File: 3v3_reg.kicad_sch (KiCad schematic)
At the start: 15 parts, among them U7 TPS62A01PDDCR

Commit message: did stuff, amongst others changed to op-amp input filter
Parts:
- D79, D81: value D_Schottky -> DSL34; LCSC (none) -> C22466347; LCSC Basic/Pref (none) -> n; LCSC Part (none) -> C22466347
- U7: footprint TPS62A01PDDCR:DDC0006A-MFG -> TPS62A01PDDCR:DDC0006A-IPC_A; LCSC (none) -> C42267816

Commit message: did stuff
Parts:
- R81, R82: LCSC Basic/Pref x -> y
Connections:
- net +5.2V renamed +5.3V
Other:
- note removed: "todo: change to C22466347"
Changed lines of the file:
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@@
 	(generator_version "10.0")
 	(paper "A4")
-	(text "todo: change to C22466347"
-		(exclude_from_sim no)
-		(at 24.384 87.376 0)
-		(effects
-			(font
-				(size 1.27 1.27)
-			)
-		)
-	)
 	(text "3.3 V Regulator"
 		(exclude_from_sim no)
@@
 		)
 	)
-	(text_box "Design Note:\nPrioritizes 5.2 V \nfrom the Ethernet PoE\nover 5.0 V from USB"
+	(text_box "Design Note:\nPrioritizes 5.3 V \nfrom the Ethernet PoE\nover 5.0 V from USB"
 		(exclude_from_sim no)
 		(at 44.45 57.15 0)
@@
 			)
 		)
-		(property "LCSC Basic/Pref" "x"
+		(property "LCSC Basic/Pref" "y"
 			(at 93.98 100.33 0)
 			(hide yes)
@@
 			)
 		)
-		(property "LCSC Basic/Pref" "x"
+		(property "LCSC Basic/Pref" "y"
 			(at 177.8 97.79 0)
 			(hide yes)
@@
 		(in_pos_files yes)
 		(dnp no)
-		(fields_autoplaced yes)
 		(property "Reference" "#PWR0324"
 			(at 43.18 83.82 0)
@@
 			)
 		)
-		(property "Value" "+5.2V"
-			(at 43.18 74.93 0)
-			(show_name no)
-			(do_not_autoplace no)
-			(effects
-				(font
-					(size 1.27 1.27)
-				)
-			)
-		)
+		(property "Value" "+5.3V"
+			(at 41.148 76.2 0)
+			(show_name no)
+			(do_not_autoplace no)
+			(effects
+				(font
+					(size 1.27 1.27)
+				)
+				(justify left)
+			)
+		)

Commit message: fixed leds
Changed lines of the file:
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@@
 	)
 	(junction
+		(at 76.2 92.71)
+		(diameter 0)
+		(color 0 0 0 0)
+	)
+	(junction
 		(at 220.98 92.71)
 		(diameter 0)
@@
 	(wire
 		(pts
+			(xy 76.2 92.71) (xy 80.01 92.71)
+		)
+		(stroke
+			(width 0)
+			(type default)
+		)
+	)
+	(wire
+		(pts
 			(xy 220.98 92.71) (xy 220.98 93.98)
 		)
@@
 	(wire
 		(pts
+			(xy 76.2 87.63) (xy 76.2 92.71)
+		)
+		(stroke
+			(width 0)
+			(type default)
+		)
+	)
+	(wire
+		(pts
 			(xy 177.8 92.71) (xy 195.58 92.71)
 		)
@@
 	(wire
 		(pts
-			(xy 63.5 92.71) (xy 80.01 92.71)
+			(xy 63.5 92.71) (xy 76.2 92.71)
 		)
 		(stroke
@@
 		)
 	)
-	(label "V3P3_VIN"
-		(at 71.12 92.71 0)
-		(effects
-			(font
-				(size 1.27 1.27)
-			)
-			(justify left bottom)
-		)
-	)
 	(label "3V3_EN"
 		(at 95.25 107.95 0)
@@
 					(unit 1)
 				)
+			)
+		)
+	)
+	(symbol
+		(lib_id "power:+3.3V")
+		(at 76.2 87.63 0)
+		(unit 1)
+		(body_style 1)
+		(exclude_from_sim no)
+		(in_bom yes)
+		(on_board yes)
+		(in_pos_files yes)
+		(dnp no)
+		(property "Reference" "#PWR0547"
+			(at 76.2 91.44 0)
+			(hide yes)
+			(show_name no)
+			(do_not_autoplace no)
+			(effects
+				(font
+					(size 1.27 1.27)
+				)
+			)
+		)
+		(property "Value" "V3P3_VIN"
+			(at 72.136 83.82 0)
+			(show_name no)
+			(do_not_autoplace no)
+			(effects
+				(font
+					(size 1.27 1.27)
+				)
+				(justify left)
+			)
+		)
+		(property "Footprint" ""
+			(at 76.2 87.63 0)
+			(hide yes)
+			(show_name no)
+			(do_not_autoplace no)
+			(effects
+				(font
+					(size 1.27 1.27)
+				)
+			)
+		)
+		(property "Datasheet" ""
+			(at 76.2 87.63 0)
+			(hide yes)
+			(show_name no)
+			(do_not_autoplace no)
+			(effects
+				(font
+					(size 1.27 1.27)
+				)
+			)
+		)
+		(property "Description" "Power symbol creates a global label with name \"+3.3V\""
+			(at 76.2 87.63 0)
+			(hide yes)
+			(show_name no)
+			(do_not_autoplace no)
+			(effects
+				(font
+					(size 1.27 1.27)
+				)
+			)
+		)
+		(pin "1"
+		)
+		(instances
+			(project "netdaq"
+				(path "/2970f661-65ab-4e2b-aeda-d76d1044f2b8/4a874178-a54c-4eb4-8350-ff261e3dfdab"
+					(reference "#PWR0547")
+					(unit 1)
+				)

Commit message: fixed a lot of review comments
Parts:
- D79: MPN (none) -> DSL34; Manufacturer (none) -> hongjiacheng
- R81, R82: Tolerance (none) -> 1%
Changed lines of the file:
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@@
 			)
 		)
-		(property "Tolerance" ""
+		(property "Tolerance" "1%"
 			(at 93.98 100.33 0)
 			(hide yes)
@@
 			)
 		)
+		(property "MPN" "DSL34"
+			(at 54.61 82.55 0)
+			(hide yes)
+			(show_name no)
+			(do_not_autoplace no)
+			(effects
+				(font
+					(size 1.27 1.27)
+				)
+			)
+		)
+		(property "Manufacturer" "hongjiacheng"
+			(at 54.61 82.55 0)
+			(hide yes)
+			(show_name no)
+			(do_not_autoplace no)
+			(effects
+				(font
+					(size 1.27 1.27)
+				)
+			)
+		)
 		(pin "1"
 		)
@@
 			)
 		)
-		(property "Tolerance" ""
+		(property "Tolerance" "1%"
 			(at 177.8 97.79 0)
 			(hide yes)

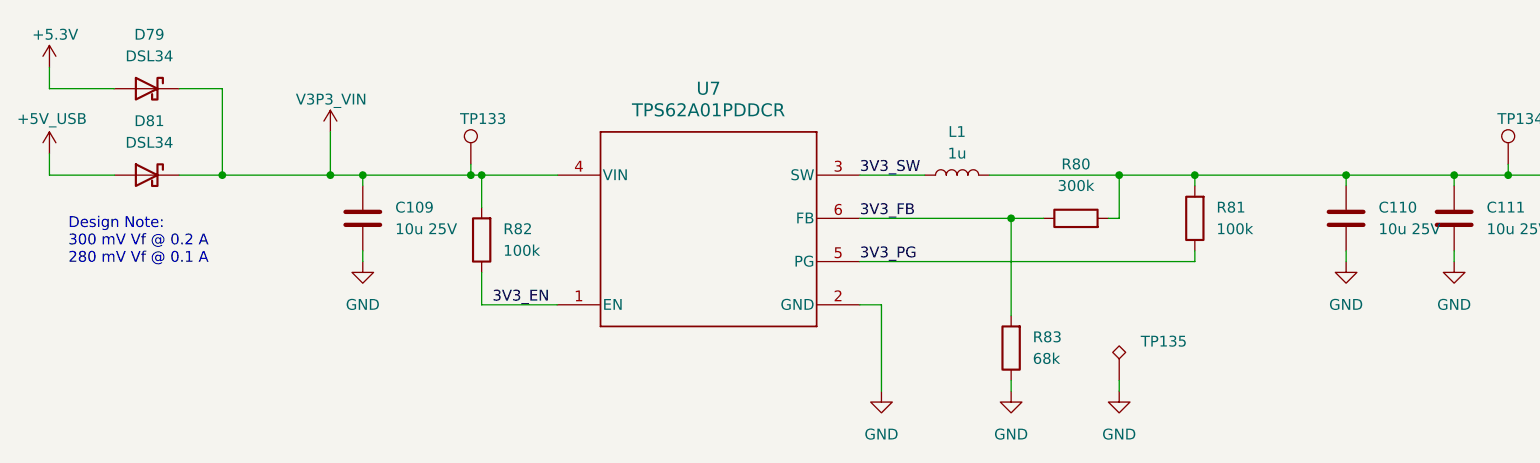
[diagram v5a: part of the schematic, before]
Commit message: fixed some more schematic review
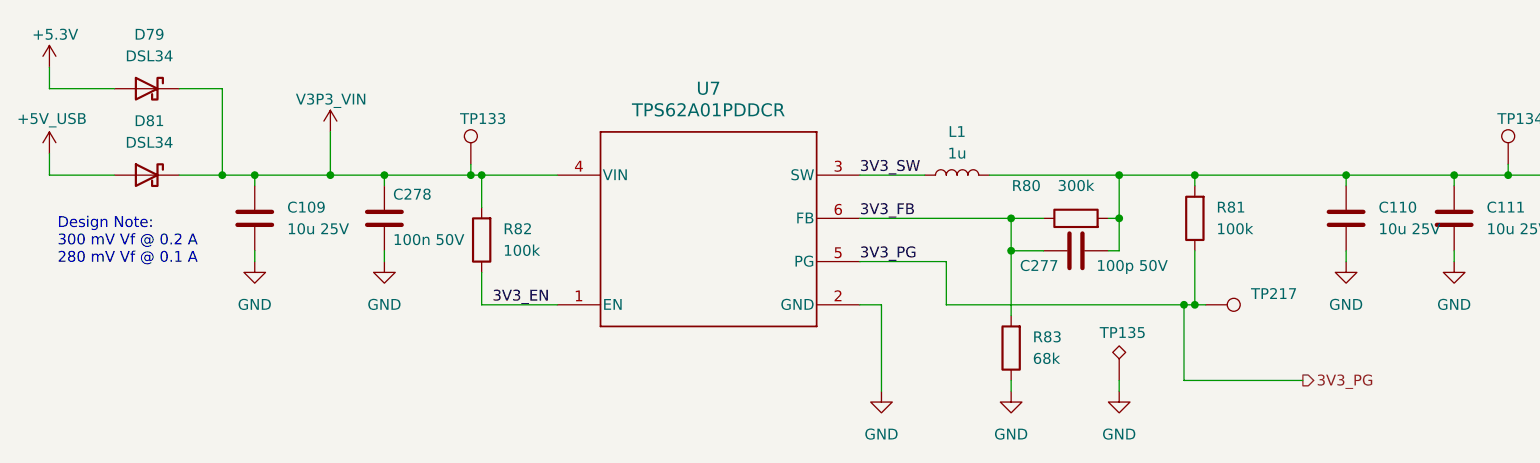
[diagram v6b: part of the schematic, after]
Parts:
- added C277: 100p 50V, Capacitor_SMD:C_0402_1005Metric, symbol Device:C
- added C278: 100n 50V, Capacitor_SMD:C_0402_1005Metric, symbol Device:C
- added TP217: TestPoint, TestPoint:TestPoint_THTPad_D1.0mm_Drill0.5mm, symbol Connector:TestPoint
- C109, C110, C111, C112: LCSC Basic/Pref x -> basic; LCSC missing (none) -> n; MPN (none) -> CL21A106KAYNNNE; Manufacturer (none) -> Samsung Electro-Mechanics; TC (none) -> X5R; Tolerance (none) -> 10%; Voltage (none) -> 25V
- D79: LCSC Basic/Pref n -> preferred; LCSC missing (none) -> n
- D81: LCSC Basic/Pref n -> preferred; LCSC missing (none) -> n; MPN (none) -> DSL34; Manufacturer (none) -> hongjiacheng
- L1: footprint Inductor_SMD:L_1210_3225Metric -> Inductor_SMD:L_1008_2520Metric; LCSC (none) -> C435392; LCSC Basic/Pref (none) -> extended; LCSC Part (none) -> C435392; LCSC missing (none) -> n; MPN (none) -> DFE252012F-1R0M=P2; Manufacturer (none) -> Murata Electronics
- R80: LCSC Basic/Pref x -> basic; LCSC missing (none) -> n; MPN (none) -> 0603WAF3003T5E; Manufacturer (none) -> UNI-ROYAL(Uniroyal Elec); Power (none) -> 100mW; Tolerance (none) -> 1%; Voltage (none) -> 75V
- R81, R82: LCSC Basic/Pref y -> basic; LCSC missing (none) -> n; MPN (none) -> 0402WGF1003TCE; Manufacturer (none) -> UNI-ROYAL(Uniroyal Elec); Power (none) -> 62.5mW; Voltage (none) -> 50V
- R83: LCSC Basic/Pref x -> basic; LCSC missing (none) -> n; MPN (none) -> 0603WAF6802T5E; Manufacturer (none) -> UNI-ROYAL(Uniroyal Elec); Power (none) -> 100mW; Tolerance (none) -> 1%; Voltage (none) -> 75V
- U7: LCSC Basic/Pref (none) -> extended; LCSC missing (none) -> n; MPN (none) -> TPS62A01PDDCR; Manufacturer (none) -> TEXAS INSTRUMENTS
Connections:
- net +3.3V: now also C277.2
- net 3V3_FB: now also C277.1
- net 3V3_PG: now also TP217.1
- net GND: now also C278.2
- net V3P3_VIN: now also C278.1
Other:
- moved on the sheet: C109

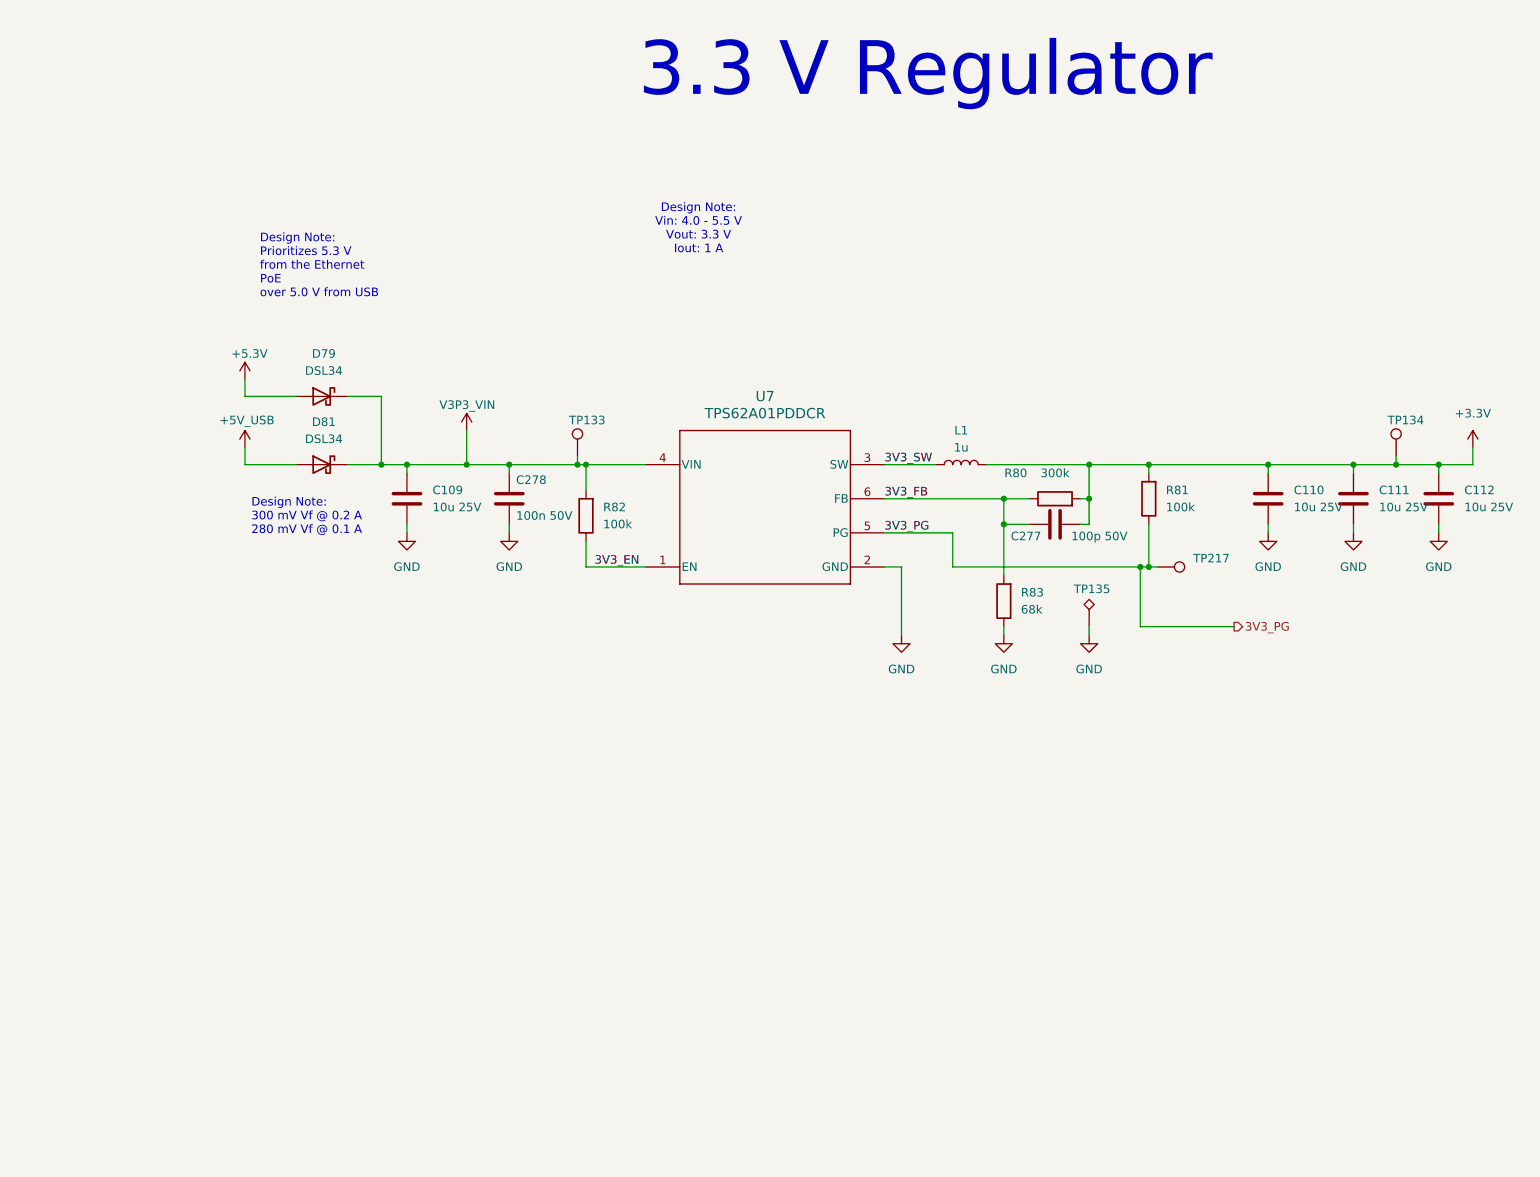
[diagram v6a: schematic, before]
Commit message: fixed some more schematic review
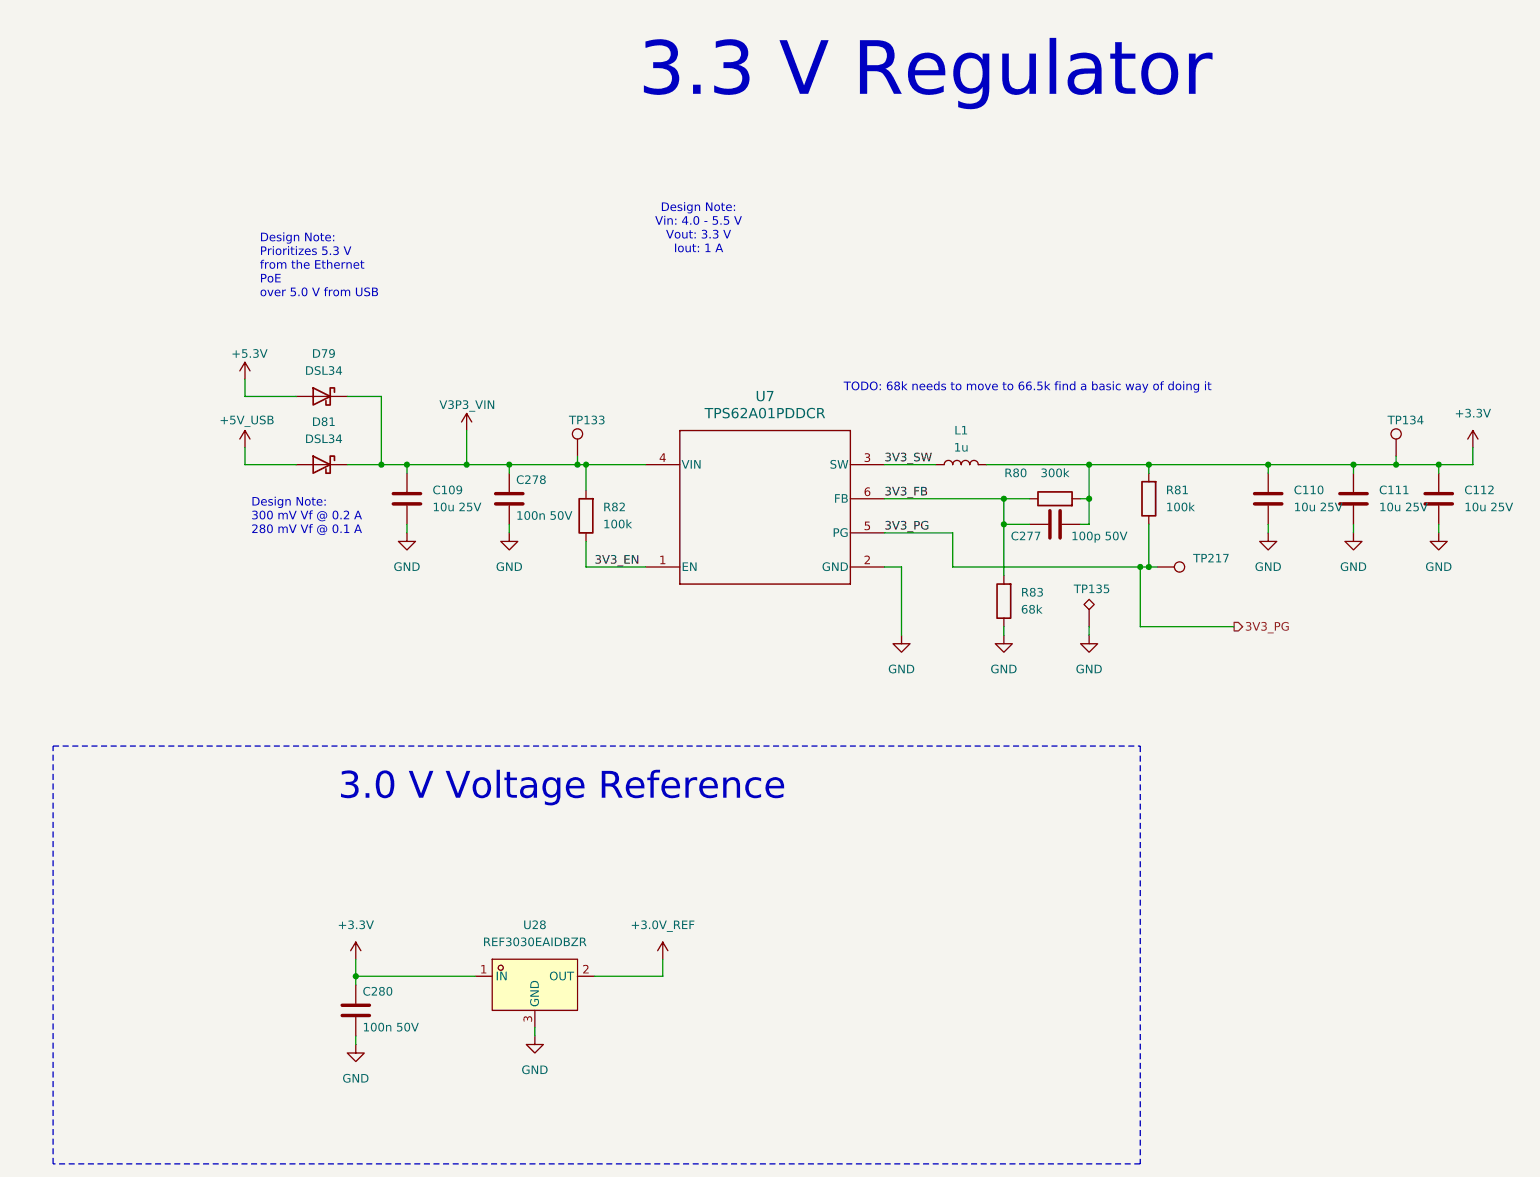
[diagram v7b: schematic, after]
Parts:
- added C280: 100n 50V, Capacitor_SMD:C_0402_1005Metric, symbol Device:C
- added U28: REF3030EAIDBZR, C54120492:SOT-23-3_L2.9-W1.3-P0.95-LS2.4-BR, symbol C54120492:REF3030EAIDBZR
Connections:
- net +3.3V: now also C280.1, U28.1 (IN)
- net GND: now also C280.2, U28.3 (GND)
- new net +3.0V_REF: U28.2 (OUT)
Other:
- note added: "3.0 V Voltage Reference"
- note added: "TODO: 68k needs to move to 66.5k find a basic way of doing it"

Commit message: did a bit of placement
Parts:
- added C285: 100n 50V, Capacitor_SMD:C_0402_1005Metric, symbol Device:C
- added R277: 200k, Resistor_SMD:R_0603_1608Metric, symbol Device:R
- R83: value 68k -> 100k; LCSC C23231 -> C25803; LCSC Part C23231 -> C25803; MPN 0603WAF6802T5E -> 0603WAF1003T5E
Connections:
- net +3.0V_REF: now also C285.1
- net 3V3_FB: now also R277.2
- net GND: now also C285.2, R277.1
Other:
- note added: "3.300 V nom, 3.198..3.405 V worst case"
- note removed: "TODO: 68k needs to move to 66.5k find a basic way of doing it"
